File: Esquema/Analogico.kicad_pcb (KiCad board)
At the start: 2 copper layers, 92.6 x 100.1 mm, 43 parts, among them J1 Conex_bat, J2 Panel Solar, J3 Galga_1, J4 Galga_2, P1 USB_C_Plug_USB2.0, U1 REF3020AIDBZT, U10 NUCLEO-F429ZI, U2 INA826AIDR, U3 TP4057, U4 INA826AIDR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

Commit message: PCB ver. 1.1 Signed-off-by: ricardo.socorro <ricardo.socorro@alumnos.upm.es>
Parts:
- moved L1 87.3 mm to (100.0, 75.0)
- moved R1 83.0 mm to (110.5, 88.2)
- moved R6 79.8 mm to (106.6, 88.0)
- moved U3 79.3 mm to (107.5, 93.3)
- moved C7 76.1 mm to (110.5, 100.0)
- moved L2 74.6 mm to (100.0, 85.5)
- moved U6 73.9 mm to (116.1, 63.5), turned to 90 degrees
- moved C4 70.9 mm to (108.0, 82.5), turned to 90 degrees
- moved R2 70.2 mm to (106.8, 100.0)
- moved C10 67.2 mm to (112.5, 82.5)
- moved R13 64.6 mm to (98.0, 93.2)
- moved C2 60.3 mm to (121.1, 88.1), turned to 90 degrees
- moved R3 59.2 mm to (116.9, 82.5), turned to 90 degrees
- moved R5 58.4 mm to (121.2, 82.5)
- moved U7 58.4 mm to (126.2, 88.0)
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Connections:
- U10 pad CN10_13: unconnected-(U10F-D26/IO-PadCN10_13) -> /EN
- U10 pad CN10_7: unconnected-(U10F-A6/ADC_A_IN-PadCN10_7) -> /ADC_V_BAT
- U10 pad CN7_20: /EN -> unconnected-(U10E-D8/IO-PadCN7_20)
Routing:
- net GND: track 525.3 -> 18.3 mm, vias 3 -> 7
- net Net-(J2-Pin_2): track 25.2 -> 128.2 mm
- net /ADC_V_BAT: track 8.28 -> 101.6 mm, vias 0 -> 1
- net Net-(D4-K): track 2.89 -> 63.1 mm, vias 0 -> 2
- net +3.3VA: track 134.0 -> 78.0 mm
- net Net-(R3-Pad1): track 4.71 -> 56.3 mm, vias 0 -> 1
- net +3.3V: track 56.0 -> 6.81 mm
- net Net-(D2-K): track 2.84 -> 45.6 mm
- net /ADC_I_BAT: track 64.3 -> 22.0 mm, vias 0 -> 1
- net /2.048: track 170.9 -> 128.8 mm, vias 1 -> 2
- net /EN: track 73.9 -> 38.1 mm, vias 1 -> 0
- net Net-(R8-Pad1): track 3.20 -> 38.7 mm
- net Net-(J1-Pin_2): track 42.3 -> 77.7 mm, vias 1 -> 2
- net /FB: track 7.63 -> 17.3 mm
- net /ADC_PESO_2: track 17.1 -> 8.31 mm, vias 1 -> 0
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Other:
- board size 92.6 x 100.1 mm -> 78 x 77.5 mm
- board text added: "+"
- board text added: "ADC_V_BAT"
- board text added: "FB"

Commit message: Placa ya terminada
Signed-off-by: ricardo.socorro <ricardo.socorro@alumnos.upm.es>
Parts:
- J1: footprint Connector_JST:JST_PH_S2B-PH-K_1x02_P2.00mm_Horizontal -> Connector_PinHeader_2.00mm:PinHeader_1x02_P2.00mm_Vertical
- moved P1 96.3 mm to (90.9, 49.5), turned to 180 degrees
- moved J2 95.7 mm to (104.2, 51.3), turned to 180 degrees
- moved R4 68.2 mm to (128.1, 62.1), turned to -90 degrees
- moved J4 66.3 mm to (97.0, 123.6), turned to 0 degrees
- moved R8 62.1 mm to (106.2, 81.1), turned to 90 degrees
- moved J3 61.6 mm to (119.1, 123.6), turned to 0 degrees
- moved C8 52.8 mm to (114.0, 105.0), turned to 90 degrees
- moved C3 48.6 mm to (99.3, 105.0), turned to 90 degrees
- moved U5 46.3 mm to (119.5, 108.3)
- moved RV1 44.2 mm to (122.9, 115.3)
- moved U2 41.9 mm to (104.9, 108.3)
- moved D4 41.0 mm to (115.6, 92.3), turned to 0 degrees
- moved RV2 40.3 mm to (108.2, 115.3)
- moved U1 30.2 mm to (95.7, 99.0), turned to 0 degrees
- moved C1 27.6 mm to (119.3, 77.1)
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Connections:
- U10 pad CN10_13: /EN -> unconnected-(U10F-D26/IO-PadCN10_13)
- U10 pad CN10_8: unconnected-(U10F-D4/IO-PadCN10_8) -> /EN
- U10 pad CN7_13: unconnected-(U10E-D22/I2S_B_SD/SPI_B_MOSI-PadCN7_13) -> /ADC_PESO_1
- U10 pad CN7_17: unconnected-(U10E-D24/SPI_B_NSS-PadCN7_17) -> /ADC_PESO_2
- U10 pad CN9_1: /ADC_PESO_1 -> unconnected-(U10D-A0/ADC123_IN3-PadCN9_1)
- U10 pad CN9_3: /ADC_PESO_2 -> unconnected-(U10D-A1/ADC123_IN10-PadCN9_3)
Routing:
- net Net-(J2-Pin_2): track 128.2 -> 35.4 mm, vias 1 -> 0
- net /ADC_V_BAT: track 101.6 -> 27.0 mm, vias 1 -> 0
- net /2.048: track 128.8 -> 63.3 mm, vias 2 -> 0
- net Net-(D4-K): track 63.1 -> 5.58 mm, vias 2 -> 0
- net Net-(R3-Pad1): track 56.3 -> 6.51 mm, vias 1 -> 0
- net Net-(J1-Pin_2): track 77.7 -> 31.4 mm, vias 2 -> 1
- net Net-(D2-K): track 45.6 -> 4.21 mm
- net Net-(R8-Pad1): track 38.7 -> 8.78 mm, vias 0 -> 1
- net /EN: track 38.1 -> 18.0 mm, vias 0 -> 1
- net GND: track 18.3 -> 0.00 mm, vias 7 -> 0
- net Net-(D1-K): track 143.7 -> 155.4 mm, vias 0 -> 2
- net /ADC_I_BAT: track 22.0 -> 13.6 mm, vias 1 -> 0
- net Net-(D3-A): track 21.3 -> 13.4 mm
- net /ADC_PESO_2: track 8.31 -> 15.8 mm, vias 0 -> 1
- net /FB: track 17.3 -> 23.3 mm
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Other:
- board size 78 x 77.5 mm -> 56.7 x 81.8 mm
- board text removed: "+"
- board text removed: "Bateria"

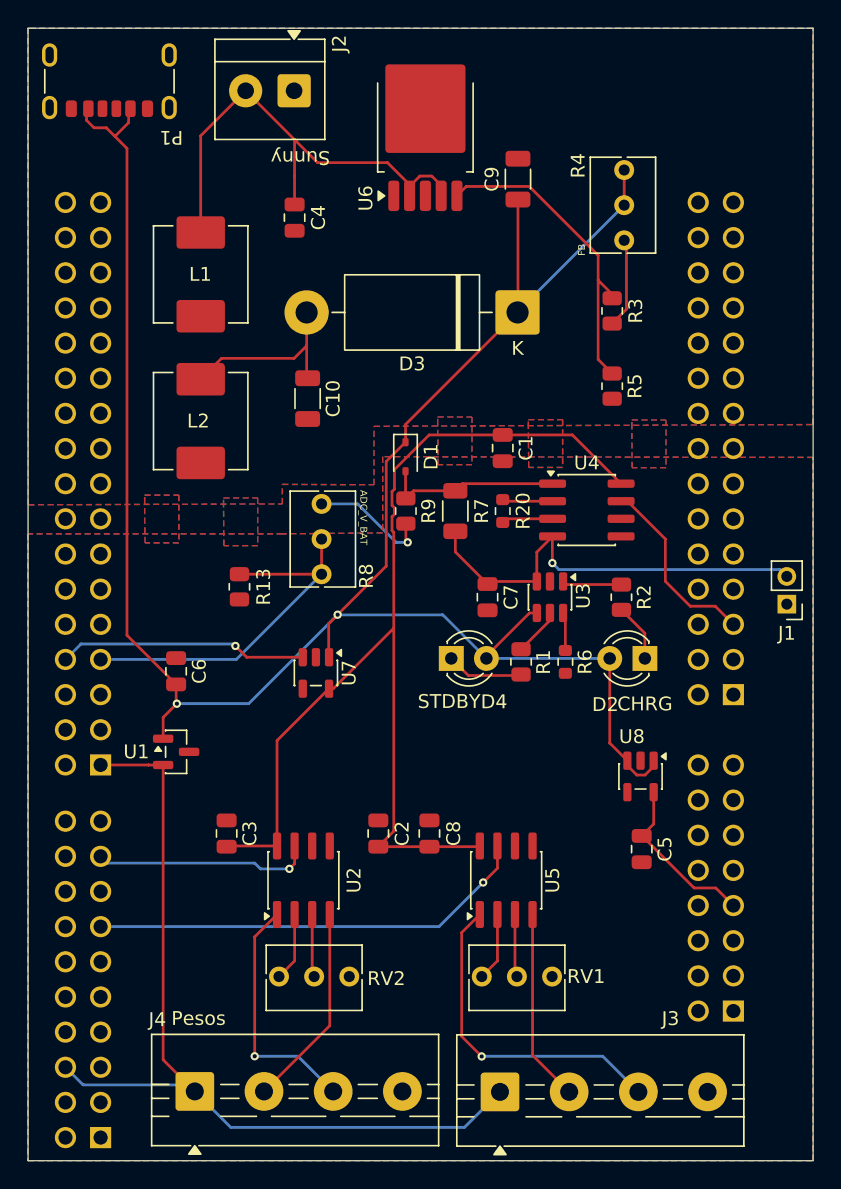
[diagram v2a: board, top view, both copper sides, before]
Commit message: añado el modo stop
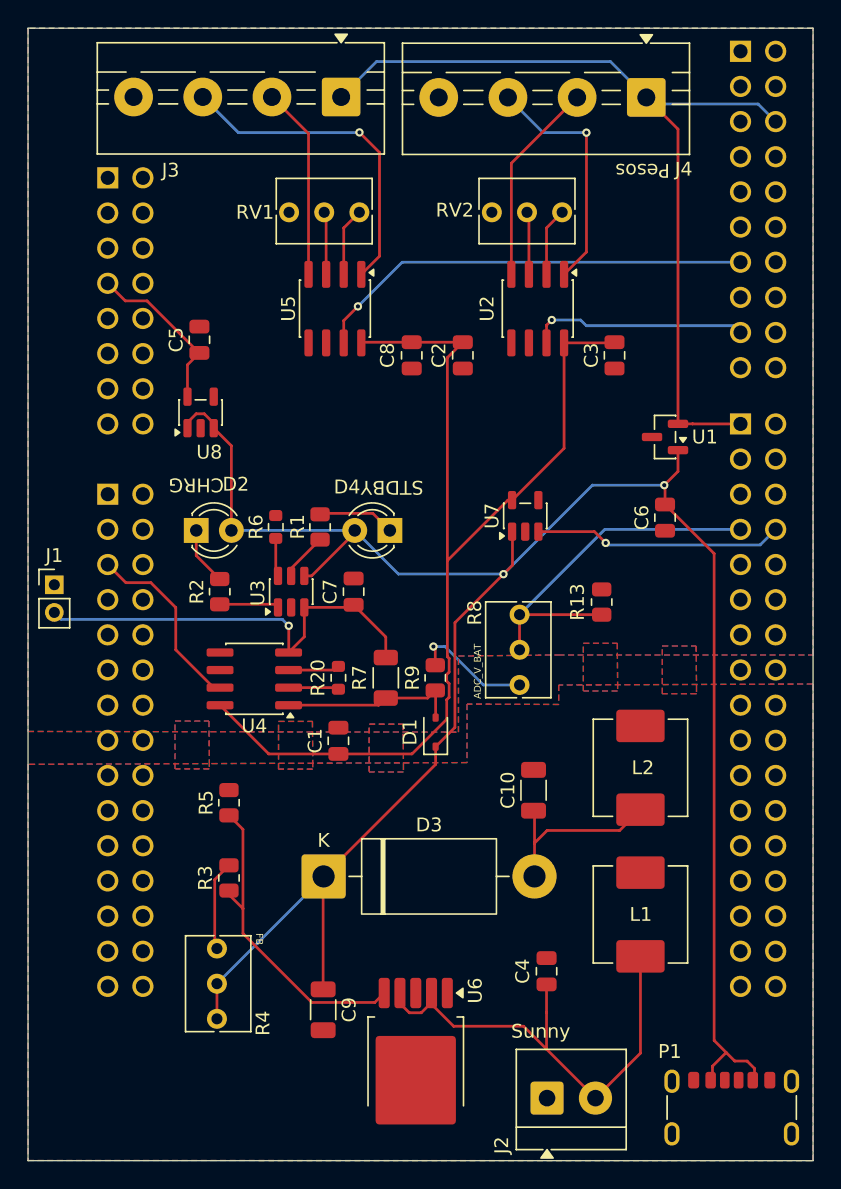
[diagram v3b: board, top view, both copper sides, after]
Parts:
- moved P1 88.6 mm to (135.8, 125.8), turned to 0 degrees
- moved J4 78.9 mm to (129.7, 51.8), turned to 180 degrees
- moved J2 75.0 mm to (122.5, 124.1), turned to 0 degrees
- moved J3 72.8 mm to (107.6, 51.7), turned to 180 degrees
- moved U6 67.7 mm to (113.0, 121.5), turned to -90 degrees
- moved C9 61.6 mm to (106.3, 117.7), turned to -90 degrees
- moved R4 59.0 mm to (98.7, 113.3), turned to 90 degrees
- moved RV1 58.4 mm to (103.9, 60.1), turned to 180 degrees
- moved C4 57.4 mm to (122.5, 114.9), turned to 90 degrees
- moved RV2 56.2 mm to (118.5, 60.1), turned to 180 degrees
- moved L1 56.1 mm to (129.2, 110.8), turned to 90 degrees
- moved J1 52.9 mm to (86.9, 87.0), turned to 0 degrees
- moved R3 49.4 mm to (99.5, 108.2), turned to -90 degrees
- moved C5 48.7 mm to (97.4, 69.3), turned to 90 degrees
- moved U2 44.6 mm to (121.8, 67.0), turned to -90 degrees
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
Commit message: Cambios en el principal y en el adc
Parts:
- moved P1 88.6 mm to (90.9, 49.5), turned to 180 degrees
- moved J4 78.9 mm to (97.0, 123.6), turned to 0 degrees
- moved J2 75.0 mm to (104.2, 51.3), turned to 180 degrees
- moved J3 72.8 mm to (119.1, 123.6), turned to 0 degrees
- moved U6 67.7 mm to (113.7, 53.8), turned to 90 degrees
- moved C9 61.6 mm to (120.4, 57.7), turned to 90 degrees
- moved R4 59.0 mm to (128.1, 62.1), turned to -90 degrees
- moved RV1 58.4 mm to (122.9, 115.3), turned to 0 degrees
- moved C4 57.4 mm to (104.3, 60.5), turned to -90 degrees
- moved RV2 56.2 mm to (108.2, 115.3), turned to 0 degrees
- moved L1 56.1 mm to (97.5, 64.5), turned to -90 degrees
- moved J1 52.9 mm to (139.8, 88.4), turned to 180 degrees
- moved R3 49.4 mm to (127.2, 67.2), turned to 90 degrees
- moved C5 48.7 mm to (129.3, 106.1), turned to -90 degrees
- moved U2 44.6 mm to (104.9, 108.3), turned to 90 degrees
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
